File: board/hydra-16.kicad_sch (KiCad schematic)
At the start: 33 parts, among them J1 Conn_01x32, J2 Conn_01x24, J3 DSUB_9, U3 AT28C64B, U4 W65C02S, U5 65C22, U6 65C51, U7 MAX232, U8 HM628512LP-5, U9 74F138

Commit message: Board V1.1G
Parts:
- added C69: 104, Capacitor_THT:C_Disc_D5.0mm_W2.5mm_P5.00mm, symbol Device:C_Small
- added J27: RDY Pull_Up, Connector_PinHeader_2.54mm:PinHeader_2x01_P2.54mm_Vertical, symbol dk_Rectangular-Connectors-Headers-Male-Pins:22-23-2021
- U8: footprint Package_DIP:DIP-32_W15.24mm_Socket_LongPads -> Package_SO:SOP-32_11.305x20.495mm_P1.27mm
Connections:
- net +5V: now also C69.1
- net A0: no longer J2.12 (Pin_12)
- net A1: no longer J2.13 (Pin_13)
- net A10: no longer J2.22 (Pin_22)
- net A11: no longer J2.23 (Pin_23)
- net A12: no longer J2.24 (Pin_24)
- net A13: no longer J1.3 (Pin_3)
- net A14: no longer J1.2 (Pin_2)
- net A15: no longer J1.1 (Pin_1)
- net A2: no longer J2.14 (Pin_14)
- net A3: no longer J2.15 (Pin_15)
- net A4: no longer J2.16 (Pin_16)
- net A5: no longer J2.17 (Pin_17)
- net A6: no longer J2.18 (Pin_18)
- net A7: no longer J2.19 (Pin_19)
- net A8: no longer J2.20 (Pin_20)
- net A9: no longer J2.21 (Pin_21)
- net D0: no longer J2.1 (Pin_1)
- net D1: no longer J2.2 (Pin_2)
- net D2: no longer J2.3 (Pin_3)
- net D3: no longer J2.4 (Pin_4)
- net D4: no longer J2.5 (Pin_5)
- net D5: no longer J2.6 (Pin_6)
- net D6: no longer J2.7 (Pin_7)
- net D7: no longer J2.8 (Pin_8)
- net GND: now also C69.2
- net RDY: now also J27.1; no longer RN1.7 (R6)
- net RWB: no longer U4.34 (R/~{W})
- new net: J27.2, RN1.7 (R6)
- new net A_MEM0: J2.12 (Pin_12)
- new net A_MEM1: J2.13 (Pin_13)
- new net A_MEM10: J2.22 (Pin_22)
- new net A_MEM11: J2.23 (Pin_23)
- new net A_MEM12: J2.24 (Pin_24)
- new net A_MEM13: J1.1 (Pin_1)
- new net A_MEM14: J1.2 (Pin_2)
- new net A_MEM15: J1.3 (Pin_3)
- new net A_MEM2: J2.14 (Pin_14)
- new net A_MEM3: J2.15 (Pin_15)
- new net A_MEM4: J2.16 (Pin_16)
- new net A_MEM5: J2.17 (Pin_17)
- new net A_MEM6: J2.18 (Pin_18)
- new net A_MEM7: J2.19 (Pin_19)
- new net A_MEM8: J2.20 (Pin_20)
- new net A_MEM9: J2.21 (Pin_21)
- new net D_MEM0: J2.1 (Pin_1)
- new net D_MEM1: J2.2 (Pin_2)
- new net D_MEM2: J2.3 (Pin_3)
- new net D_MEM3: J2.4 (Pin_4)
- new net D_MEM4: J2.5 (Pin_5)
- new net D_MEM5: J2.6 (Pin_6)
- new net D_MEM6: J2.7 (Pin_7)
- new net D_MEM7: J2.8 (Pin_8)
- new net P_RWB: U4.34 (R/~{W})
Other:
- added sheet Buffers (Buffers.kicad_sch)
- moved on the sheet: J2

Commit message: V1.2B: Final for production.
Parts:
- U3: value AT28C64B -> SST39SF010A; footprint Package_DIP:DIP-28_W15.24mm_Socket_LongPads -> Package_LCC:PLCC-32_THT-Socket; symbol Memory_EEPROM:28C256 -> Memory_Flash:SST39SF010
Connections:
- net !RWB: now also U3.24 (OE); no longer U3.22 (~{OE})
- net +5V: now also U3.31 (PGM), U3.32 (VCC); no longer U3.28 (VCC)
- net A0: now also U3.12 (A0); no longer U3.10 (A0)
- net A1: now also U3.11 (A1); no longer U3.9 (A1)
- net A10: now also U3.23 (A10); no longer U3.21 (A10)
- net A11: now also U3.25 (A11); no longer U3.23 (A11)
- net A12: now also U3.4 (A12); no longer U3.2 (A12)
- net A2: now also U3.10 (A2); no longer U3.8 (A2)
- net A3: now also U3.9 (A3); no longer U3.7 (A3)
- net A4: now also U3.8 (A4); no longer U3.6 (A4)
- net A5: now also U3.7 (A5); no longer U3.5 (A5)
- net A6: now also U3.6 (A6); no longer U3.4 (A6)
- net A7: now also U3.5 (A7); no longer U3.3 (A7)
- net A8: now also U3.27 (A8); no longer U3.25 (A8)
- net A9: now also U3.26 (A9); no longer U3.24 (A9)
- net D0: now also U3.13 (D0); no longer U3.11 (D0)
- net D1: now also U3.14 (D1); no longer U3.12 (D1)
- net D2: now also U3.15 (D2); no longer U3.13 (D2)
- net D3: now also U3.17 (D3); no longer U3.15 (D3)
- net D4: now also U3.18 (D4); no longer U3.16 (D4)
- net D5: now also U3.19 (D5); no longer U3.17 (D5)
- net D6: now also U3.20 (D6); no longer U3.18 (D6)
- net D7: now also U3.21 (D7); no longer U3.19 (D7)
- net GND: now also U3.16 (GND), U3.2 (A16), U3.28 (A13), U3.29 (A14), U3.3 (A15); no longer U3.1 (A14), U3.14 (GND), U3.26 (A13)
- net RWB: no longer U3.27 (~{WE})
- net nOSR_S: now also U3.22 (CE); no longer U3.20 (~{CS})
- no-connect marks 7 -> 9
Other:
- moved on the sheet: C6

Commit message: V1.3 Initial (preliminary) checkin
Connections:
- net GND: no longer U3.2 (A16), U3.28 (A13), U3.29 (A14), U3.3 (A15)
- new net W0: U3.28 (A13)
- new net W1: U3.29 (A14)
- new net W2: U3.3 (A15)
- new net W3: U3.2 (A16)

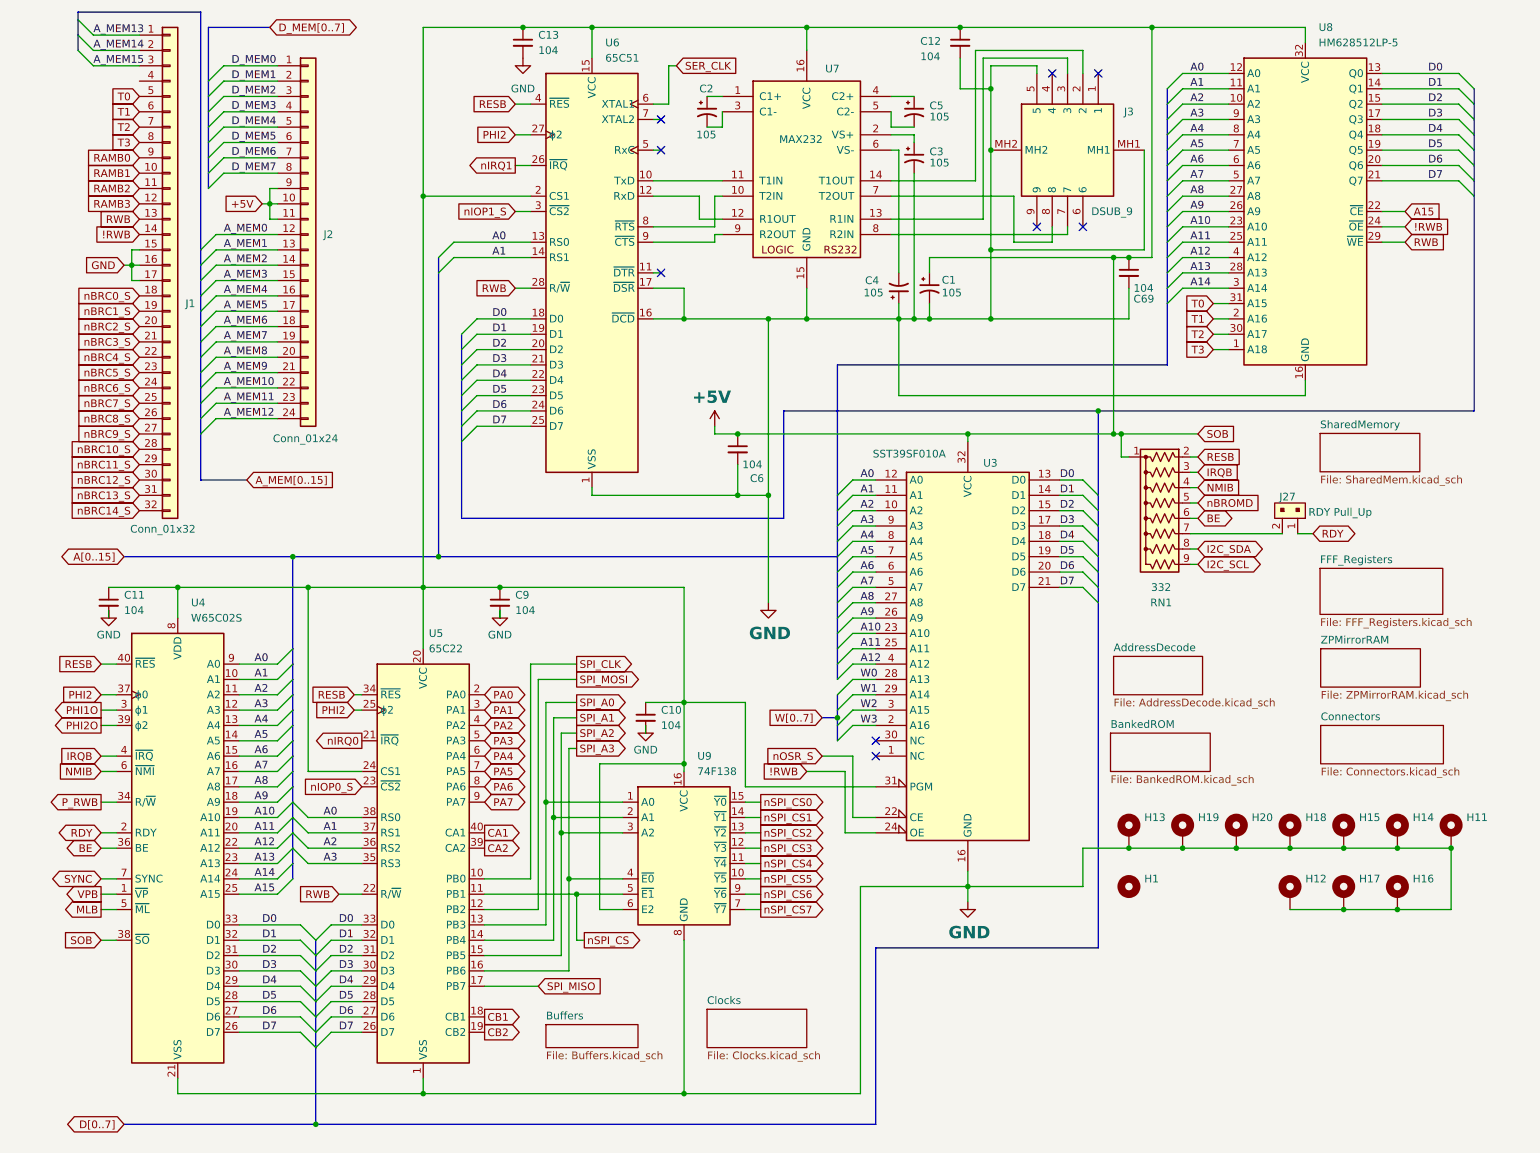
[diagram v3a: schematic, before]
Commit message: V1.3C without board traces
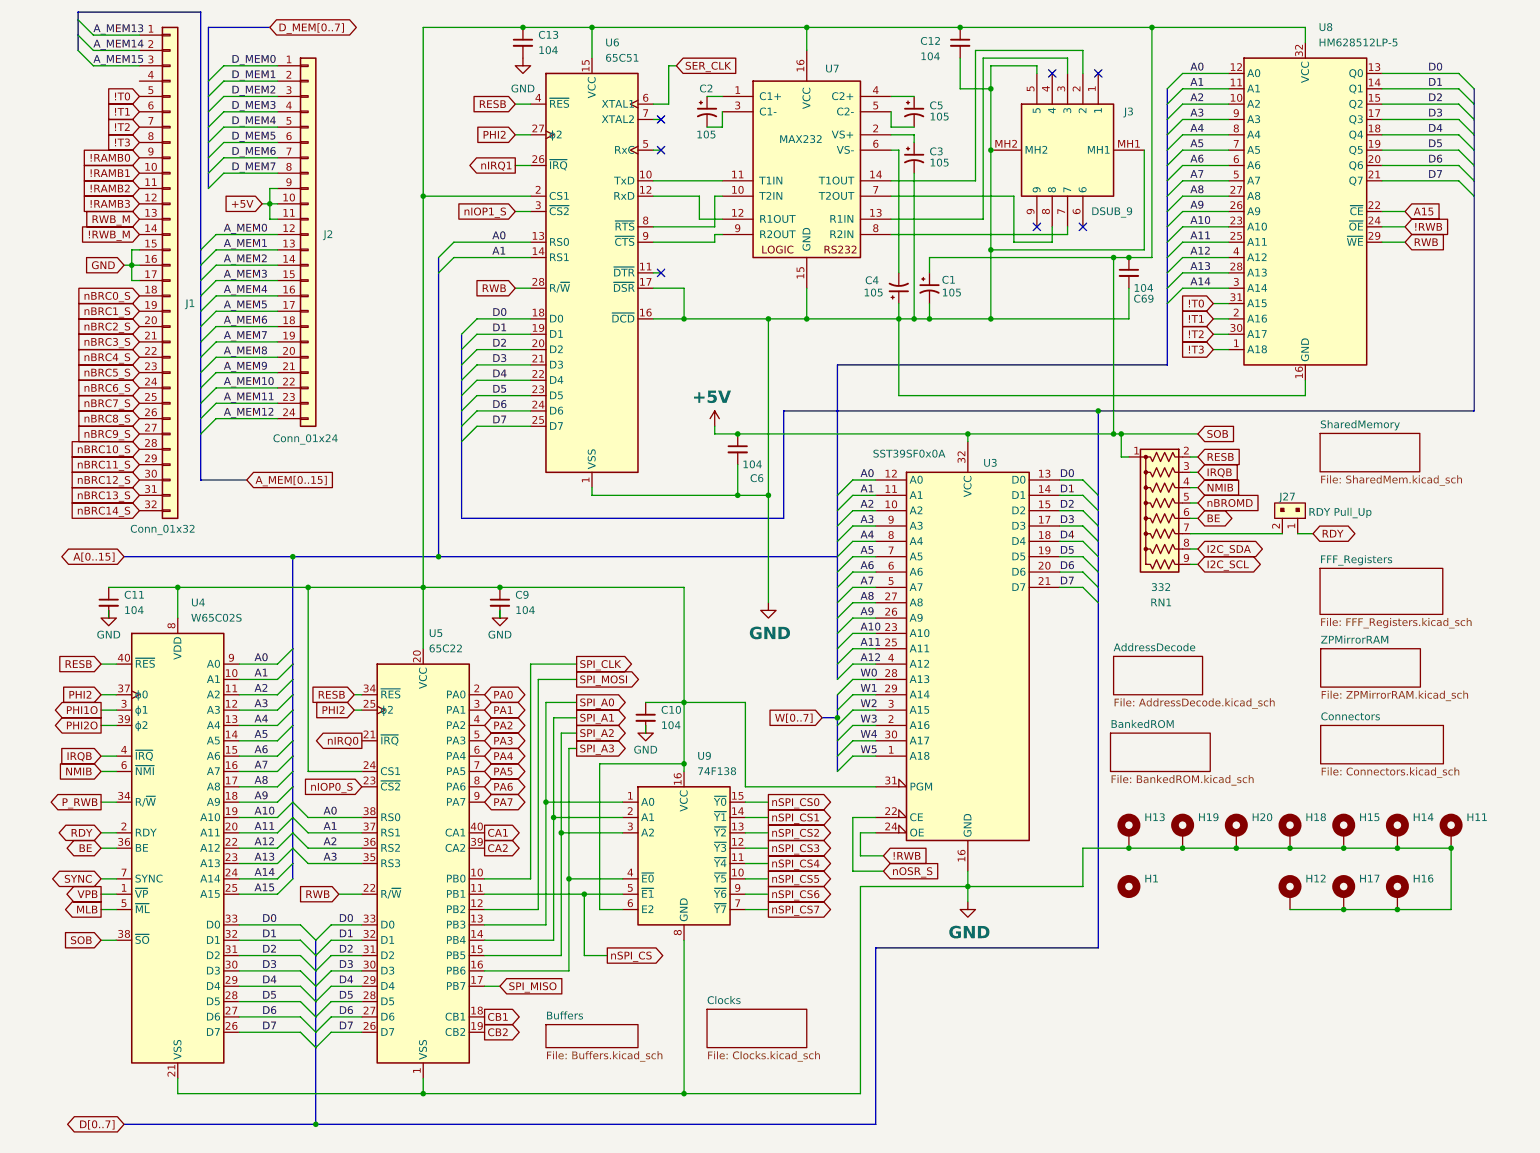
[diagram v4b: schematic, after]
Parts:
- U3: value SST39SF010A -> SST39SF0x0A
- U8: footprint Package_SO:SOP-32_11.305x20.495mm_P1.27mm -> Package_DIP:DIP-32_W15.24mm_Socket_LongPads
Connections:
- net !RWB: no longer J1.14 (Pin_14)
- net RWB: no longer J1.13 (Pin_13)
- net W5: now reaches U3.1 (A18)
- net W4: now reaches U3.30 (A17)
- net RAMB0 renamed !RAMB0
- net RAMB1 renamed !RAMB1
- net RAMB2 renamed !RAMB2
- net RAMB3 renamed !RAMB3
- net T0 renamed !T0
- net T1 renamed !T1
- net T2 renamed !T2
- net T3 renamed !T3
- new net !RWB_M: J1.14 (Pin_14)
- new net RWB_M: J1.13 (Pin_13)
- no-connect marks 9 -> 7

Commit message: V1.4E
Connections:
- net A_MEM0 is gone; now on net A0: J2.12 (Pin_12)
- net A_MEM1 is gone; now on net A1: J2.13 (Pin_13)
- net A_MEM10 is gone; now on net A10: J2.22 (Pin_22)
- net A_MEM11 is gone; now on net A11: J2.23 (Pin_23)
- net A_MEM12 is gone; now on net A12: J2.24 (Pin_24)
- net A_MEM13 is gone; now on net A13: J1.1 (Pin_1)
- net A_MEM14 is gone; now on net A14: J1.2 (Pin_2)
- net A_MEM15 is gone; now on net A15: J1.3 (Pin_3)
- net A_MEM2 is gone; now on net A2: J2.14 (Pin_14)
- net A_MEM3 is gone; now on net A3: J2.15 (Pin_15)
- net A_MEM4 is gone; now on net A4: J2.16 (Pin_16)
- net A_MEM5 is gone; now on net A5: J2.17 (Pin_17)
- net A_MEM6 is gone; now on net A6: J2.18 (Pin_18)
- net A_MEM7 is gone; now on net A7: J2.19 (Pin_19)
- net A_MEM8 is gone; now on net A8: J2.20 (Pin_20)
- net A_MEM9 is gone; now on net A9: J2.21 (Pin_21)
- net D_MEM0 is gone; now on net D0: J2.1 (Pin_1)
- net D_MEM1 is gone; now on net D1: J2.2 (Pin_2)
- net D_MEM2 is gone; now on net D2: J2.3 (Pin_3)
- net D_MEM3 is gone; now on net D3: J2.4 (Pin_4)
- net D_MEM4 is gone; now on net D4: J2.5 (Pin_5)
- net D_MEM5 is gone; now on net D5: J2.6 (Pin_6)
- net D_MEM6 is gone; now on net D6: J2.7 (Pin_7)
- net D_MEM7 is gone; now on net D7: J2.8 (Pin_8)
- net A0: no longer U4.9 (A0)
- net A1: no longer U4.10 (A1)
- net A10: no longer U4.19 (A10)
- net A11: no longer U4.20 (A11)
- net A12: no longer U4.22 (A12)
- net A13: no longer U4.23 (A13)
- net A14: no longer U4.24 (A14)
- net A15: no longer U4.25 (A15)
- net A2: no longer U4.11 (A2)
- net A3: no longer U4.12 (A3)
- net A4: no longer U4.13 (A4)
- net A5: no longer U4.14 (A5)
- net A6: no longer U4.15 (A6)
- net A7: no longer U4.16 (A7)
- net A8: no longer U4.17 (A8)
- net A9: no longer U4.18 (A9)
- net D0: no longer U4.33 (D0)
- net D1: no longer U4.32 (D1)
- net D2: no longer U4.31 (D2)
- net D3: no longer U4.30 (D3)
- net D4: no longer U4.29 (D4)
- net D5: no longer U4.28 (D5)
- net D6: no longer U4.27 (D6)
- net D7: no longer U4.26 (D7)
- net PA0: now also U4.9 (A0)
- net PA1: now also U4.10 (A1)
- net PA2: now also U4.11 (A2)
- net PA3: now also U4.12 (A3)
- net PA4: now also U4.13 (A4)
- net PA5: now also U4.14 (A5)
- net PA6: now also U4.15 (A6)
- net PA7: now also U4.16 (A7)
- new net PA10: U4.19 (A10)
- new net PA11: U4.20 (A11)
- new net PA12: U4.22 (A12)
- new net PA13: U4.23 (A13)
- new net PA14: U4.24 (A14)
- new net PA15: U4.25 (A15)
- new net PA8: U4.17 (A8)
- new net PA9: U4.18 (A9)
- new net PD0: U4.33 (D0)
- new net PD1: U4.32 (D1)
- new net PD2: U4.31 (D2)
- new net PD3: U4.30 (D3)
- new net PD4: U4.29 (D4)
- new net PD5: U4.28 (D5)
- new net PD6: U4.27 (D6)
- new net PD7: U4.26 (D7)
